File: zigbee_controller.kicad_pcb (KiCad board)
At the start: 2 copper layers, 55.5 x 62.9 mm, 74 parts, among them J1 KF635, J10 TerminalBlock_KF301-5.0, J11 TerminalBlock_KF301-5.0, J12 TerminalBlock_KF301-5.0, J13 TerminalBlock_KF301-5.0, J3 Conn_01x06, J4 Conn_01x07, J5 Conn_01x05, P1 USB_C_Receptacle_GCT_USB4105, Q2 IRLB3813, Q3 IRLB3813, Q4 IRLB3813, Q5 IRLB3813, SW2 EN, SW4 Boot, U1 TPS54560, U2 ESP32-C6-MINI-1, U4 TC4427, U5 TC4427, U6 RT9080, U9 CH224K

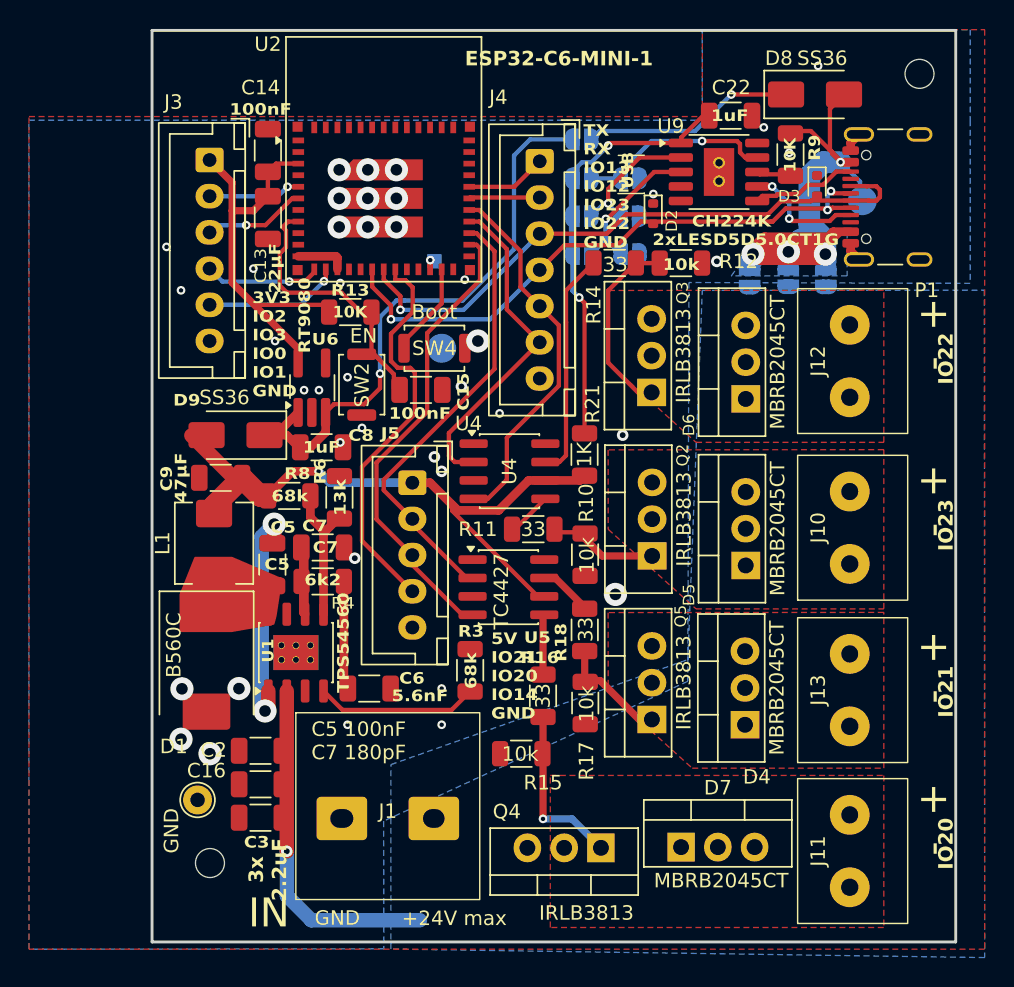
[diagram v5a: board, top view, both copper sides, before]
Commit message: Massive optimization of ground plane for high voltage path
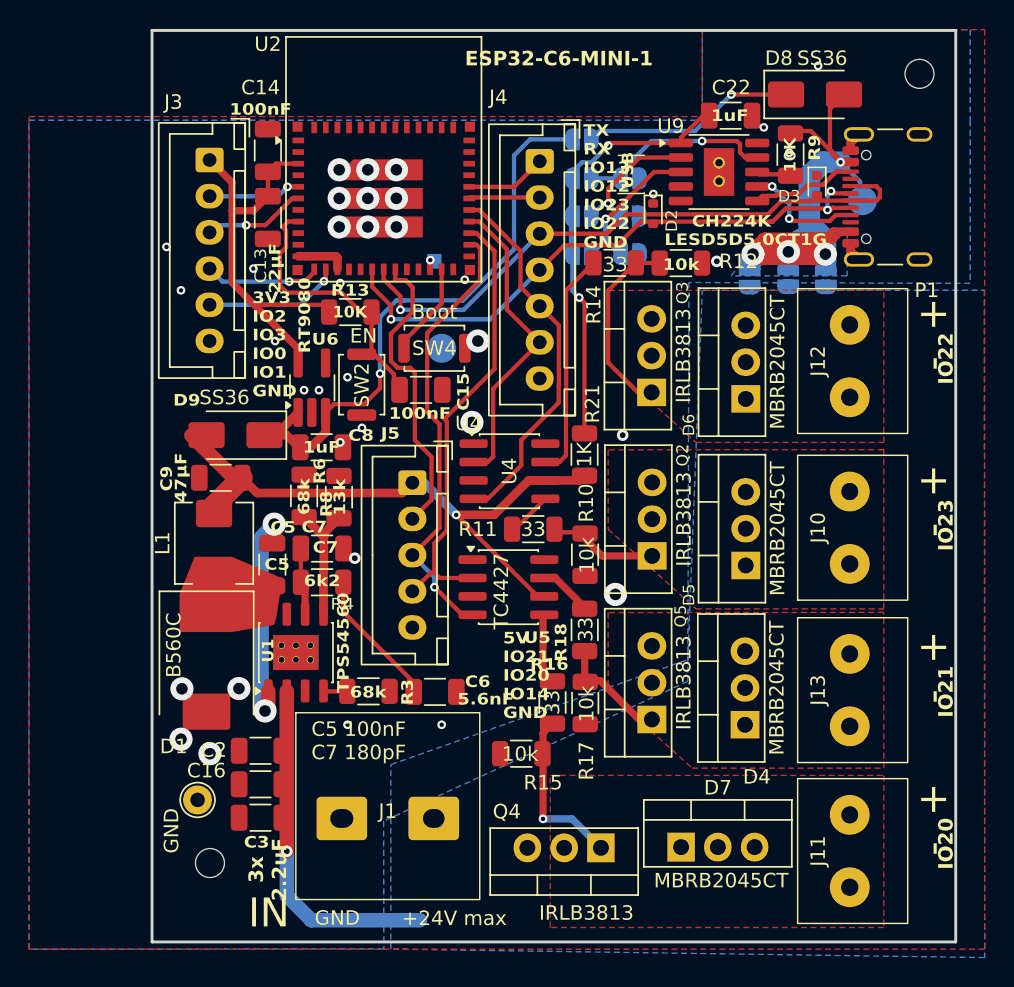
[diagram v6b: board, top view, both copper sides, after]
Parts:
- D3: value 2xLESD5D5.0CT1G -> LESD5D5.0CT1G
- JP6: value CFG1-H / power via terminal -> power_via_terminal(CFG1-H)
- JP8: value power via terminal* -> power_via_terminal
- moved R3 7.17 mm to (167.4, 115.6), turned to 0 degrees
- moved C6 4.55 mm to (172.0, 115.7)
- moved R8 1.03 mm to (163.0, 102.1), turned to -90 degrees
- moved R16 0.80 mm to (180.2, 116.4)
- moved C7 0.09 mm to (164.2, 105.8)
- moved R4 0.07 mm to (164.2, 108.1)
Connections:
- J5 pad 2: /IO21 -> /IO14
- J5 pad 4: /IO14 -> /IO21
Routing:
- net Net-(U1-RT/CLK): track 11.2 -> 1.65 mm
- net /IO14: track 27.9 -> 20.9 mm
- net Net-(U1-COMP): track 8.85 -> 4.13 mm
- net Net-(C6-Pad1): track 7.12 -> 9.58 mm
- net /IO22: track 23.1 -> 21.5 mm
- net /IO21: track 30.0 -> 31.5 mm
- net Net-(U1-FB): track 10.0 -> 9.00 mm
- net /IO20: track 30.9 -> 30.4 mm, vias 0 -> 1
- net GND: vias 40 -> 36

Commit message: Fixed termal relieve zone
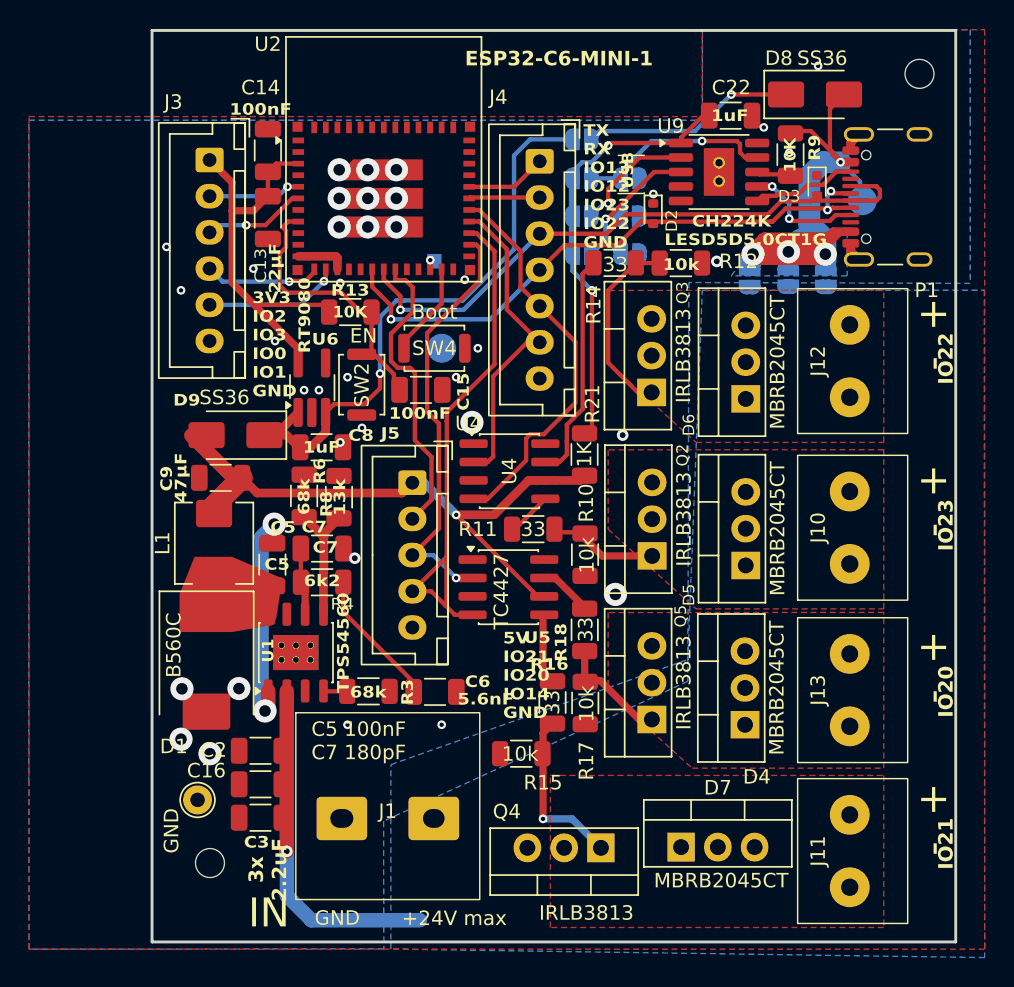
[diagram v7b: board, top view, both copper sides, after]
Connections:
- U5 pad 2: /IO21 -> /IO20
- U5 pad 4: /IO20 -> /IO21
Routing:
- net /IO21: track 31.5 -> 36.3 mm
- net /IO23: track 25.9 -> 27.4 mm
- net /IO20: track 30.4 -> 29.5 mm
- net /IO22: track 21.5 -> 22.0 mm
- net GND: vias 36 -> 37

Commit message: All errors and warning fixed
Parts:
- moved R21 2.16 mm to (182.4, 101.5)
- moved R8 0.09 mm to (163.0, 102.2)
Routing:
- net /CH224k_Vdd: track 30.3 -> 32.4 mm
- net Net-(U2-EN): track 20.5 -> 19.5 mm
- net +5V: track 43.7 -> 44.4 mm
